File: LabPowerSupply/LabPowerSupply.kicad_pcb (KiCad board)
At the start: 2 copper layers, 208 parts, among them Q1_LVR1 PJA3404_R1_00001, Q1_LVR2 PJA3404_R1_00001, Q2_LVR1 PJA3404_R1_00001, Q2_LVR2 PJA3404_R1_00001, Q3_LVR1 PJA3404_R1_00001, Q3_LVR2 PJA3404_R1_00001, SW11 Decimal, SW12 0, SW13 Backspace, SW14 Current 2, SW15 Cancel, SW21 1, SW22 2, SW23 3, SW24 Voltage 2, SW25 Confirm, SW31 4, SW32 5, SW33 6, SW34 Current 1, SW35 Channel 2, SW41 7, SW42 8, SW43 9, SW44 Voltage 1, SW45 Channel 1, Y1 8M, Y2 8M

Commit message: just a commit
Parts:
- R11_OA1, R11_OA2: value 4k -> 10k
- moved D1_CP1 9.92 mm to (135.9, 62.4)
- moved C1_CP1 9.92 mm to (120.7, 62.4)
- moved D2_CP1 9.92 mm to (130.8, 72.6)
- moved R_CP1 9.92 mm to (151.1, 62.4)
- moved C2_CP1 9.92 mm to (148.6, 68.6)
- moved Q_CP1 9.92 mm to (156.2, 68.6)
- moved C3_CP1 9.92 mm to (141.0, 73.7)
- moved C2_Y1 2.84 mm to (304.8, 38.1)
- moved C1_Y1 2.54 mm to (304.8, 31.8)
- moved Front_Panel1 1.80 mm to (268.7, 162.6)
- moved J_USB1 1.80 mm to (280.7, 138.4)
- moved R_CC1 1.80 mm to (279.2, 146.1)
- moved R_CC2 1.80 mm to (278.1, 130.8)
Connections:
- Inverter1 pad 10: (no net) -> unconnected-(Inverter1-Pad10)
- Inverter1 pad 11: (no net) -> unconnected-(Inverter1-Pad11)
- Inverter1 pad 12: (no net) -> unconnected-(Inverter1-Pad12)
- Inverter1 pad 13: (no net) -> unconnected-(Inverter1-Pad13)
- Inverter1 pad 3: (no net) -> unconnected-(Inverter1-Pad3)
- Inverter1 pad 4: (no net) -> unconnected-(Inverter1-Pad4)
- Inverter1 pad 5: (no net) -> unconnected-(Inverter1-Pad5)
- Inverter1 pad 6: (no net) -> unconnected-(Inverter1-Pad6)
- Inverter1 pad 8: (no net) -> unconnected-(Inverter1-Pad8)
- Inverter1 pad 9: (no net) -> unconnected-(Inverter1-Pad9)
- Inverter2 pad 10: (no net) -> unconnected-(Inverter2-Pad10)
- Inverter2 pad 11: (no net) -> unconnected-(Inverter2-Pad11)
- Inverter2 pad 12: (no net) -> unconnected-(Inverter2-Pad12)
- Inverter2 pad 13: (no net) -> unconnected-(Inverter2-Pad13)
- Inverter2 pad 8: (no net) -> unconnected-(Inverter2-Pad8)
- Inverter2 pad 9: (no net) -> unconnected-(Inverter2-Pad9)

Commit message: Actually updated pcb
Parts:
- C10_Power1, C1_Power1, C1_Power2, C2_Power1, C2_Power2, C3_Power1, C3_Power2, C4_Power1, C4_Power2, C5_Power1, C5_Power2, C6_Power1, C6_Power2, C7_Power1, C7_Power2, C8_Power1, C8_Power2, C9_Power1: footprint Capacitor_THT:C_Disc_D5.0mm_W2.5mm_P2.50mm -> Capacitor_SMD:C_0603_1608Metric
- C3_LVR1, C3_LVR2, C4_LVR1, C4_LVR2: footprint Capacitor_THT:C_Disc_D5.0mm_W2.5mm_P2.50mm -> Capacitor_THT:C_Disc_D7.5mm_W2.5mm_P5.00mm
- C3_SVR1, C3_SVR2: footprint Capacitor_THT:C_Disc_D7.0mm_W2.5mm_P5.00mm -> Capacitor_THT:C_Disc_D7.5mm_W2.5mm_P5.00mm
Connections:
- Inverter1 pad 11: unconnected-(Inverter1-Pad11) -> GND1
- Inverter1 pad 13: unconnected-(Inverter1-Pad13) -> GND1
- Inverter1 pad 3: unconnected-(Inverter1-Pad3) -> GND1
- Inverter1 pad 5: unconnected-(Inverter1-Pad5) -> GND1
- Inverter1 pad 9: unconnected-(Inverter1-Pad9) -> GND1
- Inverter2 pad 11: unconnected-(Inverter2-Pad11) -> GND2
- Inverter2 pad 13: unconnected-(Inverter2-Pad13) -> GND2
- Inverter2 pad 9: unconnected-(Inverter2-Pad9) -> GND2

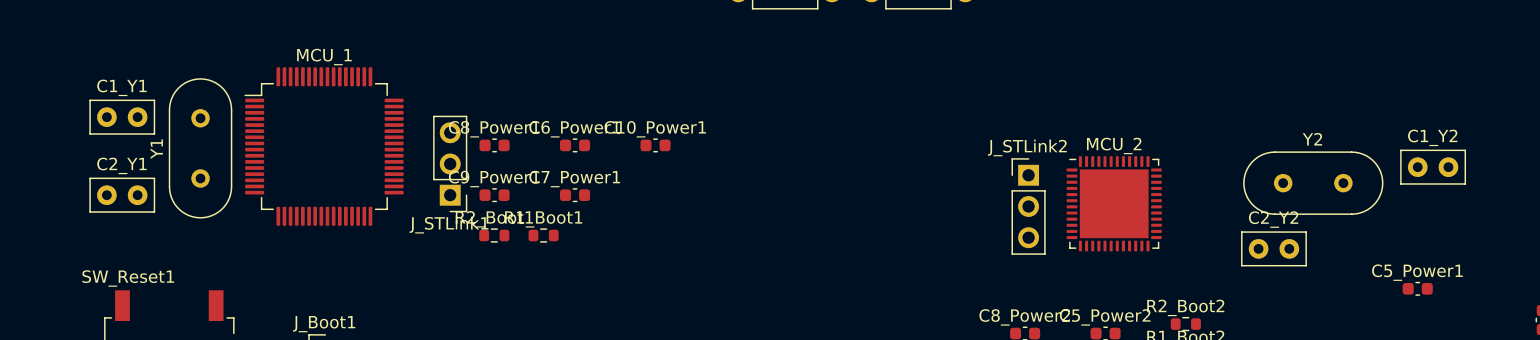
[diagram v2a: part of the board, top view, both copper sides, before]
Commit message: Made oscillator caps smd
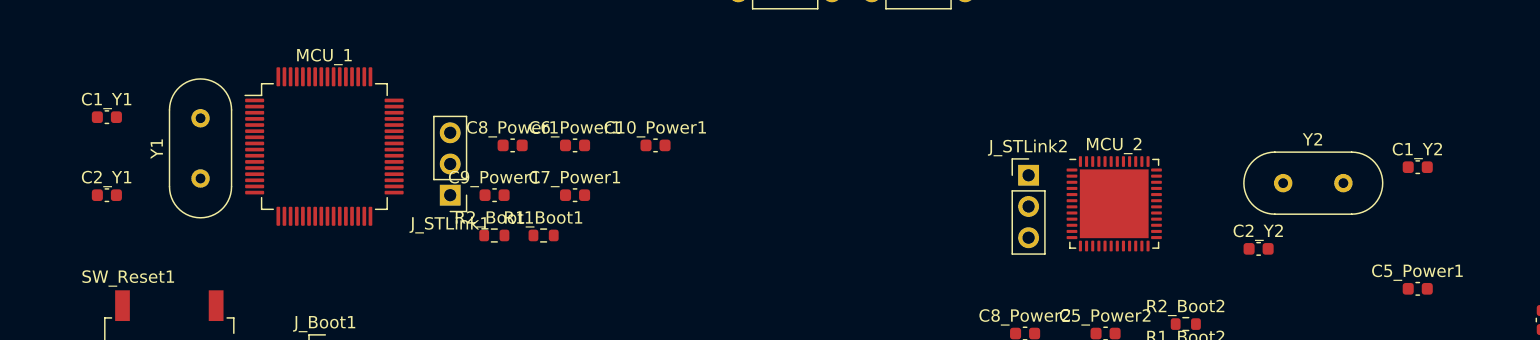
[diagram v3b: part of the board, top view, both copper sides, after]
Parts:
- C1_Y1, C1_Y2, C2_Y1, C2_Y2: footprint Capacitor_THT:C_Disc_D5.0mm_W2.5mm_P2.50mm -> Capacitor_SMD:C_0603_1608Metric
- moved C8_Power1 1.47 mm to (337.8, 34.0)

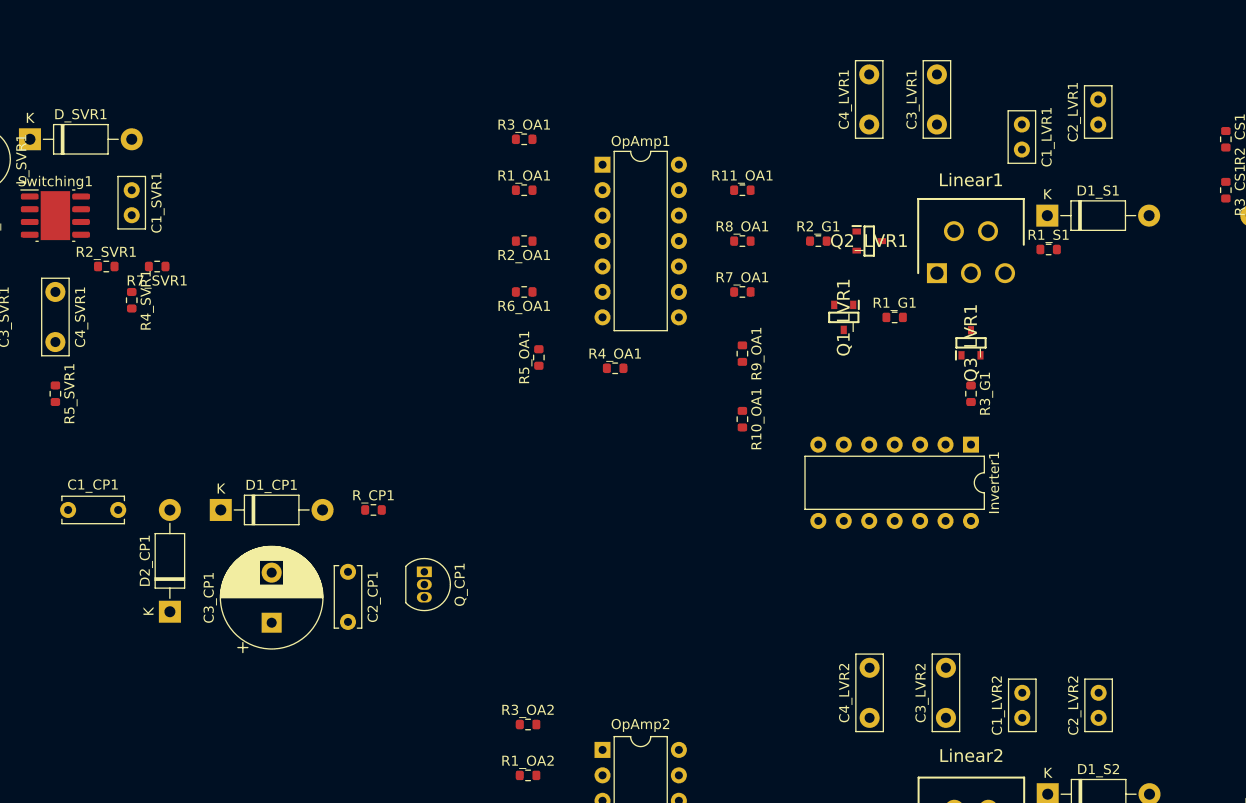
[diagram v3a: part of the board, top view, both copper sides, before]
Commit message: fixed linear cap footprints
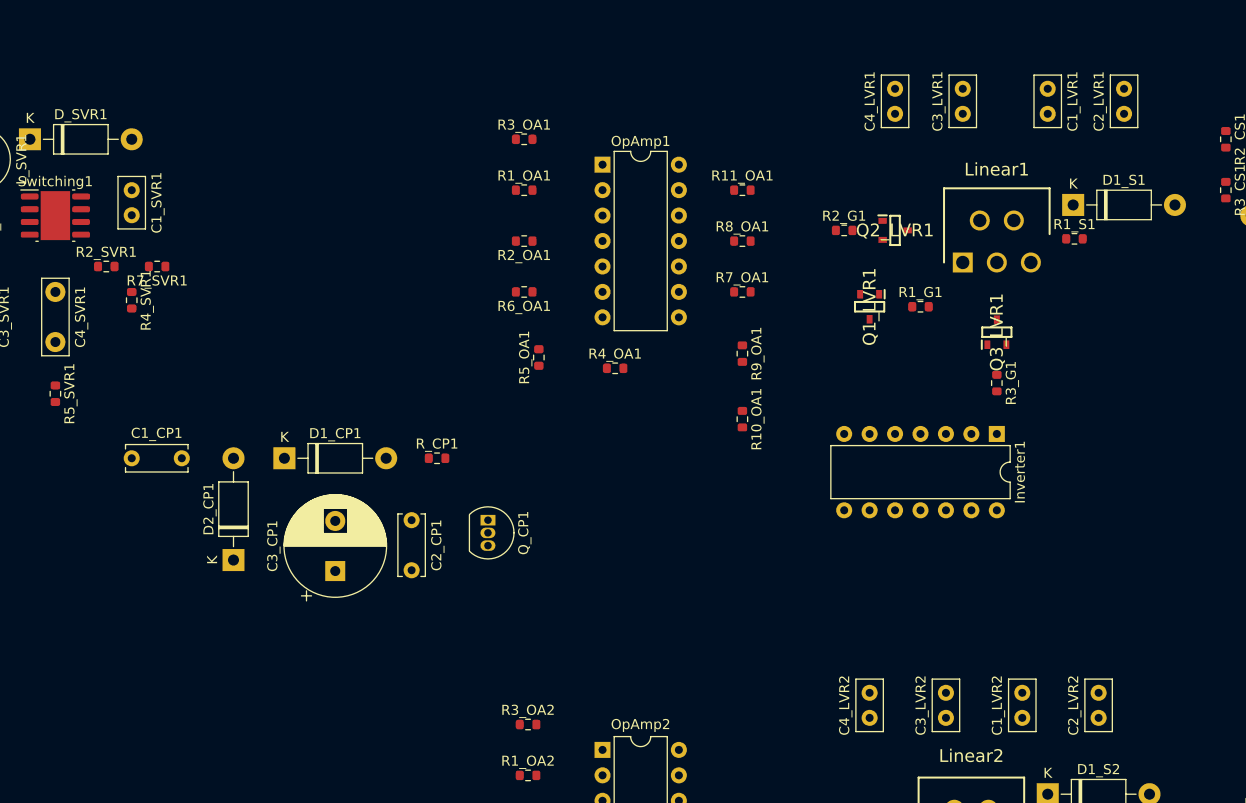
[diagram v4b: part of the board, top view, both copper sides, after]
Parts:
- C3_LVR1, C3_LVR2, C4_LVR1, C4_LVR2: footprint Capacitor_THT:C_Disc_D7.5mm_W2.5mm_P5.00mm -> Capacitor_THT:C_Disc_D5.0mm_W2.5mm_P2.50mm
- moved D1_CP1 8.18 mm to (142.2, 57.2)
- moved D2_CP1 8.18 mm to (137.2, 67.4)
- moved C1_CP1 8.18 mm to (127.0, 57.2)
- moved R_CP1 8.18 mm to (157.5, 57.2)
- moved C2_CP1 8.18 mm to (154.9, 63.4)
- moved C3_CP1 8.18 mm to (147.3, 68.5)
- moved Q_CP1 8.18 mm to (162.6, 63.4)
- moved C1_LVR1 4.40 mm to (218.4, 20.4)
- moved Inverter1 2.79 mm to (213.4, 54.8)
- moved R2_G1 2.79 mm to (198.1, 34.5)
- moved C2_LVR1 2.79 mm to (226.1, 22.9)
- moved Q3_LVR1 2.79 mm to (213.4, 44.7)
- moved R1_G1 2.79 mm to (205.7, 42.1)
- moved R1_S1 2.79 mm to (221.1, 35.3)
- moved R3_G1 2.79 mm to (213.4, 49.7)
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
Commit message: Changed most parts to smd
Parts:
- added C4_CP1: 22u, Capacitor_SMD:C_0805_2012Metric, F.Cu at (142.6, 71.9)
- added C4_CP3: 22u, Capacitor_SMD:C_0805_2012Metric, F.Cu at (142.6, 115.1)
- added C5_CP1: 1m, Capacitor_THT:CP_Radial_D10.0mm_P5.00mm, F.Cu at (132.1, 76.2)
- added C5_CP2: 1m, Capacitor_THT:CP_Radial_D10.0mm_P5.00mm, F.Cu at (132.1, 119.4)
- added Linear1_1: LT3080xDD, Package_DFN_QFN:DFN-8-1EP_3x3mm_P0.5mm_EP1.66x2.38mm, F.Cu at (226.1, 45.7)
- added Linear2_1: LT3080xDD, Package_DFN_QFN:DFN-8-1EP_3x3mm_P0.5mm_EP1.66x2.38mm, F.Cu at (221.0, 104.1)
- C10_Power1, C1_Power1, C1_Power2, C1_Y1, C1_Y2, C2_Power1, C2_Power2, C2_Y1, C2_Y2, C3_Power1, C3_Power2, C4_Power1, C4_Power2, C5_Power1, C5_Power2, C6_Power1, C6_Power2, C7_Power1, C7_Power2, C8_Power1, C8_Power2, C9_Power1: footprint Capacitor_SMD:C_0603_1608Metric -> Capacitor_SMD:C_0805_2012Metric
- C1_3.3V1, C1_3.3V2, C1_LVR1, C1_LVR2, C1_SVR1, C1_SVR2, C2_3.3V2, C2_LVR1, C2_LVR2, C3_LVR1, C3_LVR2, C4_LVR1, C4_LVR2, C_3V1: footprint Capacitor_THT:C_Disc_D5.0mm_W2.5mm_P2.50mm -> Capacitor_SMD:C_0805_2012Metric
- C1_CP1, C1_CP2, C2_CP1, C2_CP2: value 47u -> 22u; footprint Capacitor_THT:C_Disc_D6.0mm_W2.5mm_P5.00mm -> Capacitor_SMD:C_0805_2012Metric
- C2_5V1: footprint Capacitor_THT:C_Disc_D6.0mm_W2.5mm_P5.00mm -> Capacitor_SMD:C_0805_2012Metric
- C3_CP1, C3_CP2: value 1m -> 22u; footprint Capacitor_THT:CP_Radial_D10.0mm_P5.00mm -> Capacitor_SMD:C_0805_2012Metric
- C3_SVR1, C3_SVR2, C4_SVR1, C4_SVR2: footprint Capacitor_THT:C_Disc_D7.5mm_W2.5mm_P5.00mm -> Capacitor_SMD:C_0805_2012Metric
- D1_BR1, D1_BR2, D2_BR1, D2_BR2, D3_BR1, D3_BR2, D4_BR1, D4_BR2: value SB130 -> PMEG4050EP; footprint Diode_THT:D_DO-41_SOD81_P10.16mm_Horizontal -> Diode_SMD:D_SOD-128
- D1_CP1, D1_CP2, D1_S1, D1_S2, D2_CP1, D2_CP2, D_5V1, D_CS1, D_CS2, D_SVR1, D_SVR2: value SB130 -> 1N4001; footprint Diode_THT:D_DO-41_SOD81_P10.16mm_Horizontal -> Diode_SMD:D_SMA
- F_CS1, F_CS2: footprint Fuse:Fuseholder_Littelfuse_100_series_5x20mm -> Fuse:Fuse_1812_4532Metric
- Inverter1, Inverter2: footprint Package_DIP:DIP-14_W7.62mm -> Package_SO:SSOP-14_5.3x6.2mm_P0.65mm
- OpAmp1, OpAmp2: footprint Package_DIP:DIP-14_W7.62mm -> Package_SO:SOIC-14_3.9x8.7mm_P1.27mm
- Optocoupler1, Optocoupler2: footprint Package_DIP:DIP-8_W7.62mm -> Package_DIP:PowerIntegrations_SMD-8
- U_3.3V1, U_3.3V2: footprint Package_TO_SOT_THT:TO-92_Inline -> Package_TO_SOT_SMD:TO-252-3_TabPin4
- moved C2_CP2 13.0 mm to (147.3, 104.1)
- moved R_CP2 13.0 mm to (147.3, 96.5)
- moved C3_CP2 13.0 mm to (137.2, 109.2)
- moved D1_CP2 13.0 mm to (132.1, 96.5)
- moved Q_CP2 13.0 mm to (154.9, 104.1)
- moved D2_CP2 13.0 mm to (127.0, 106.7)
- moved C1_CP2 8.03 mm to (121.9, 101.6)
- moved C1_CP1 5.08 mm to (132.1, 57.2)
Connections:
- C2_CP1 pad 1: /Channel Power Supply 1/Charge Pump/Negative -> /Channel Power Supply 1/AC 1
- C2_CP1 pad 2: GND1 -> Net-(C1_CP1-Pad2)
- C2_CP2 pad 1: /Channel Power Supply 2/Charge Pump/Negative -> /Channel Power Supply 2/AC 1
- C2_CP2 pad 2: GND2 -> Net-(C1_CP2-Pad2)
- C3_CP1 pad 1: GND1 -> /Channel Power Supply 1/Charge Pump/Negative
- C3_CP1 pad 2: /Channel Power Supply 1/Charge Pump/Negative -> GND1
- C3_CP2 pad 1: GND2 -> /Channel Power Supply 2/Charge Pump/Negative
- C3_CP2 pad 2: /Channel Power Supply 2/Charge Pump/Negative -> GND2

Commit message: Fixed oscillator caps, began changing resistors to more common values
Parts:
- added R8_SVR1: 1.2k, Resistor_SMD:R_0603_1608Metric, F.Cu at (134.6, 33.0)
- added R8_SVR2: 1.2k, Resistor_SMD:R_0603_1608Metric, F.Cu at (112.6, 111.8)
- C1_Y1, C1_Y2, C2_Y1, C2_Y2: value 100n -> 20p; footprint Capacitor_SMD:C_0805_2012Metric -> Capacitor_SMD:C_0603_1608Metric
- R4_SVR1, R4_SVR2: value 2.4k -> 1.2k
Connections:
- R4_SVR1 pad 1: /Channel Power Supply 1/Switching Voltage Regulator/FeedBack -> Net-(R4_SVR1-Pad1)
- R4_SVR2 pad 1: /Channel Power Supply 2/Switching Voltage Regulator/FeedBack -> Net-(R4_SVR2-Pad1)
